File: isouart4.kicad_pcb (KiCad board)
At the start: 2 copper layers, 89 x 99 mm, 86 parts, among them J1 USB_B, J2 Conn_01x04, J3 Conn_01x04, J4 Conn_01x04, J5 Conn_01x04, U1 AMS1117-3.3, U10 74HC123, U11 74HC123, U2 π122U31, U3 π122U31, U4 π122U31, U5 π122U31, U7 CH344Q, U8 74HC123, U9 74HC123, Y1 8MHz

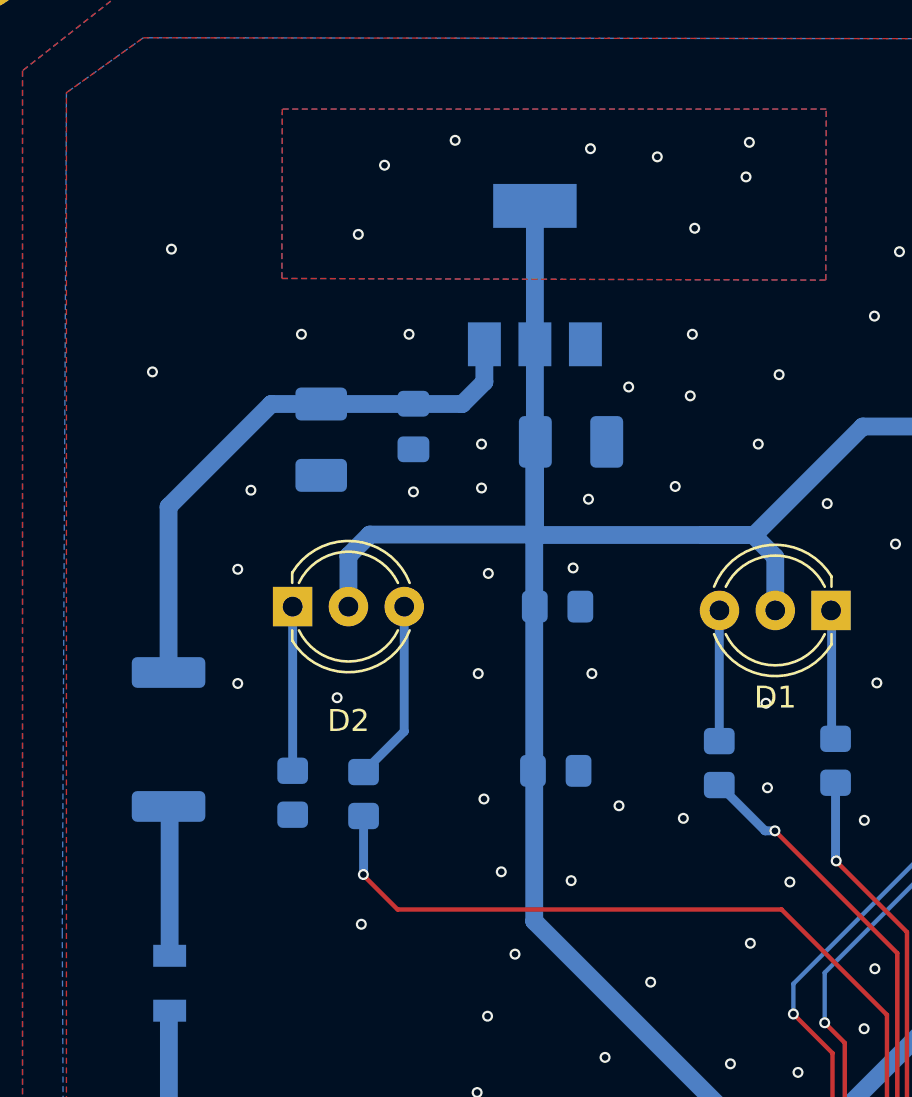
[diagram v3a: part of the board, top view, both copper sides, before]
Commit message: AMS1117-3.3 -> LP2950CDT-3.3 (reduce usb downstream capacitance)
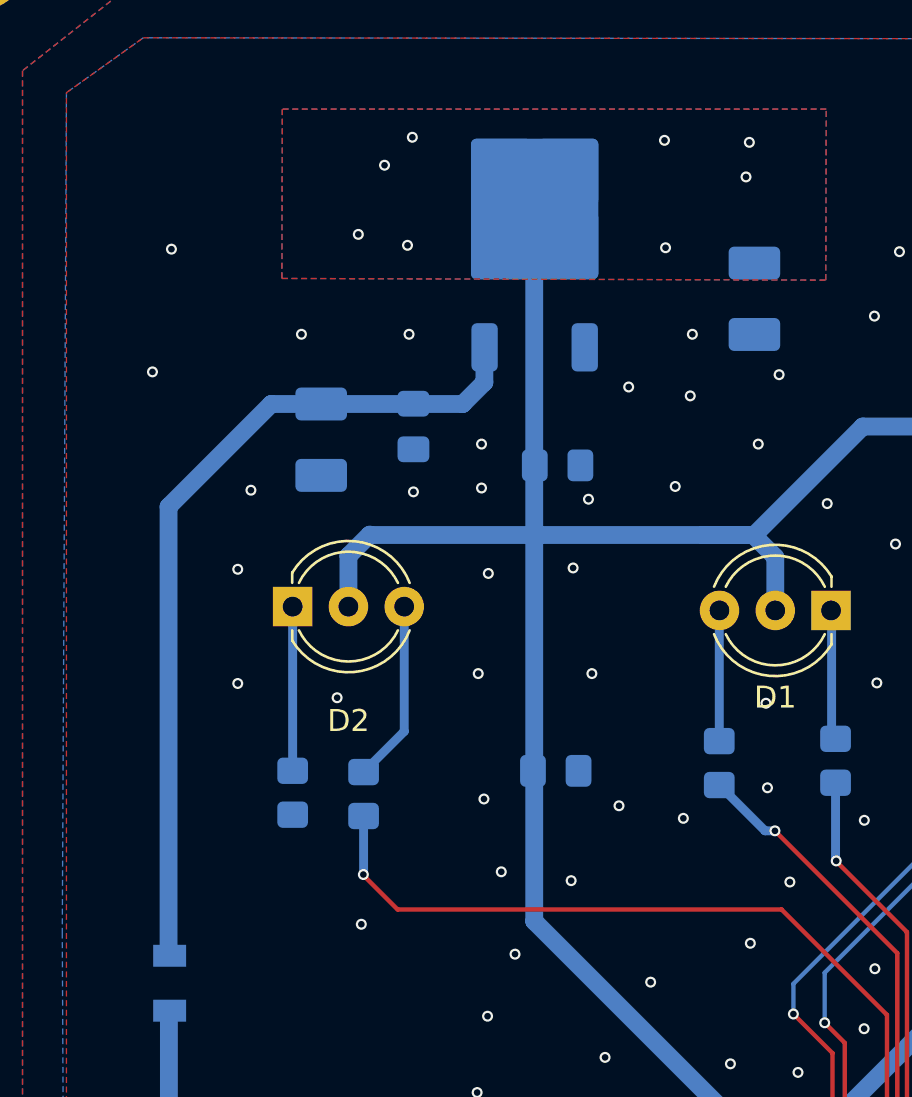
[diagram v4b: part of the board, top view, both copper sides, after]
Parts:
- removed R26: 4R3, Resistor_SMD:R_2512_6332Metric_Pad1.40x3.35mm_HandSolder
- C1: value 10uF -> 1uF
- C2: value 22uF -> 3.3uF
- F1: value 500mA -> 100mA
- U1: value AMS1117-3.3 -> LP2950CDT-3.3; footprint Package_TO_SOT_SMD:SOT-223-3_TabPin2 -> Package_TO_SOT_SMD:TO-252-2
- moved C2 10.6 mm to (179.3, 59.4), turned to -90 degrees
- moved C31 6.43 mm to (170.4, 67.0)
- moved U1 1.75 mm to (169.3, 56.6)
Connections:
- FB1 pad 1: Net-(FB1-Pad1) -> Net-(U1-VI)
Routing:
- net Net-(U1-VI): track 26.0 -> 39.0 mm
- net Net-(FB1-Pad1): track 6.82 -> 0.00 mm
- net /USB-UART4-CH344Q/VIN 3.3V: track 175.4 -> 171.5 mm

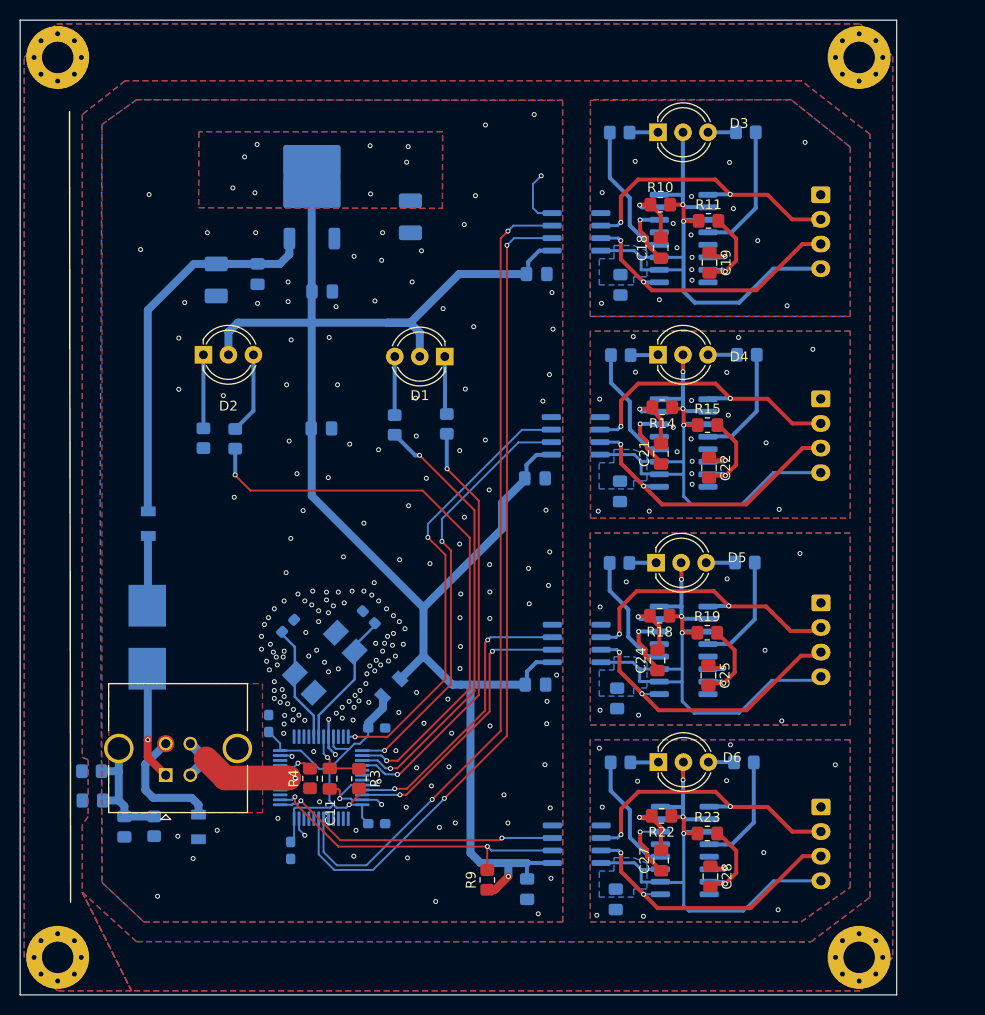
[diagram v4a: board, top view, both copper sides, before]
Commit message: adjust silkscreen and led positions; reannotate
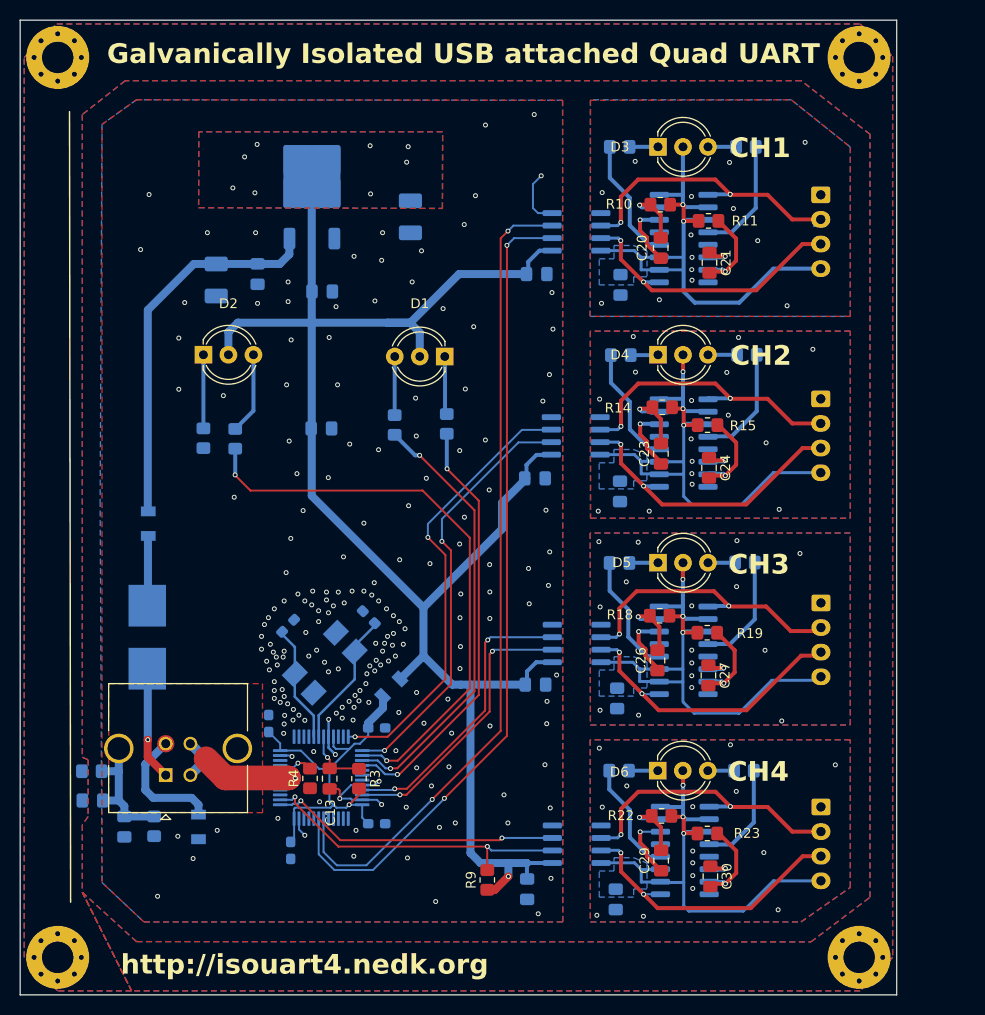
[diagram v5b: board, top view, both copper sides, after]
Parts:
- moved D3 1.48 mm to (204.5, 52.3)
- moved R12 1.48 mm to (213.4, 52.3)
- moved R13 1.46 mm to (200.6, 52.3)
- moved D6 0.87 mm to (204.4, 115.6)
- moved R25 0.85 mm to (200.5, 115.6)
- moved R24 0.84 mm to (213.2, 115.6)
- moved D5 0.19 mm to (204.5, 94.5)
- renumbered C8 to C10, C10 to C12, C11 to C13, C12 to C14, C13 to C15, C14 to C16, C15 to C17, C17 to C18, C16 to C19, C30 to C2, C18 to C20, C19 to C21, C20 to C22, C21 to C23, C22 to C24, C23 to C25, C24 to C26, C25 to C27, C26 to C28, C27 to C29, C31 to C3, C28 to C30, C29 to C31, C2 to C4, C3 to C5, C4 to C6, C5 to C7, C6 to C8, C7 to C9
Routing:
- net /indicators-ch1/V+MON: track 56.7 -> 55.2 mm
- net Net-(U8A-~{Q}): track 13.6 -> 12.1 mm
- net Net-(U8B-~{Q}): track 14.1 -> 12.6 mm
- net Net-(U11A-~{Q}): track 11.7 -> 10.8 mm
- net /indicators-ch4/V+MON: track 52.3 -> 51.5 mm
- net Net-(U11B-~{Q}): track 12.3 -> 11.5 mm
- net /indicators-ch4/GNDMON: vias 10 -> 15
- net /indicators-ch3/GNDMON: vias 8 -> 16
- net /indicators-ch2/GNDMON: vias 18 -> 16
- net /indicators-ch1/GNDMON: vias 16 -> 14
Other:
- board text added: "CH1"
- board text added: "CH2"
- board text added: "CH3"
- board text added: "CH4"
- board text added: "Galvanically Isolated USB attached Quad UART"
- board text added: "http://isouart4.nedk.org"

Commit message: Add OSHW logo
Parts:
- added REF1: OSHW, isouart4:OSHW, F.Cu at (149.9, 100.1)

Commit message: Adjust OSHW logo to have footprint and use it
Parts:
- removed REF1: OSHW, isouart4:OSHW
- added LOGO1: OSHW, isouart4:OSHW, F.Cu at (150.3, 99.9)

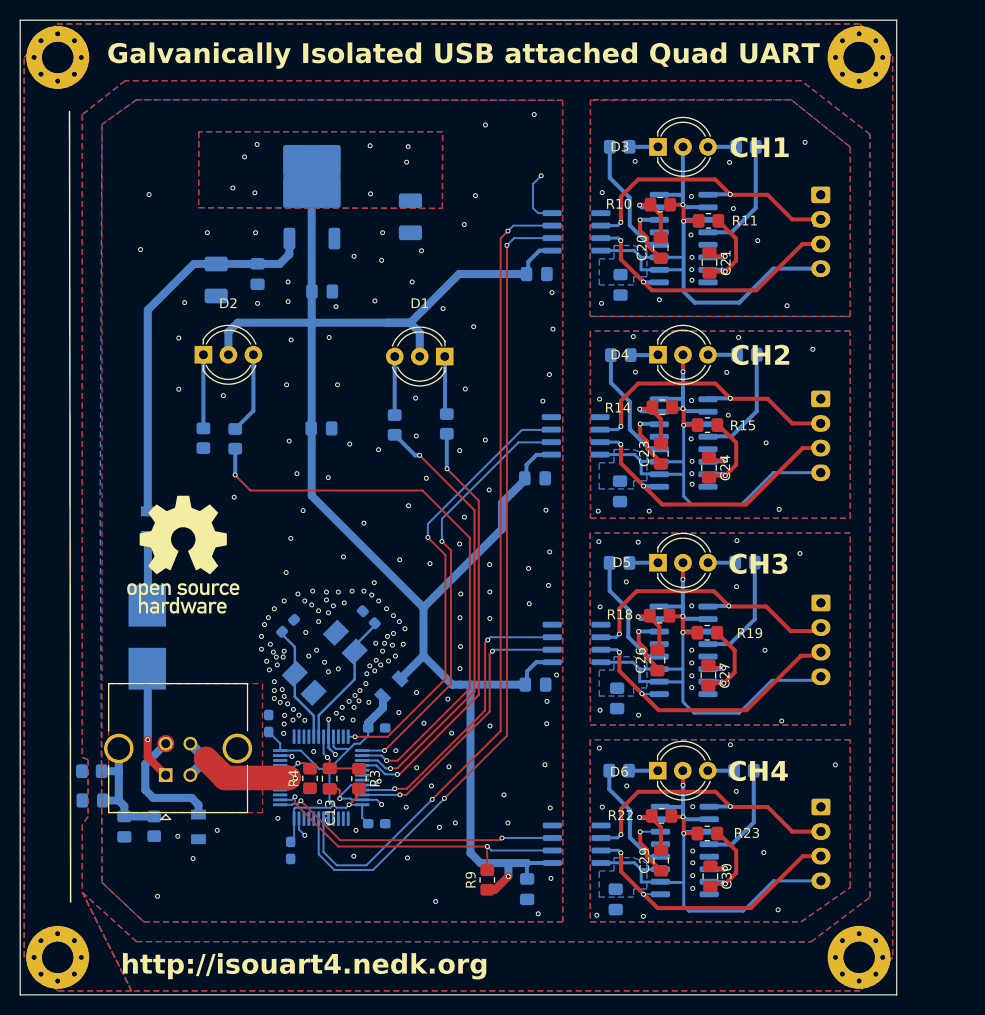
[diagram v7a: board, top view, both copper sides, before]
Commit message: increase via size to 0.6mm and via annular width to 0.13mm
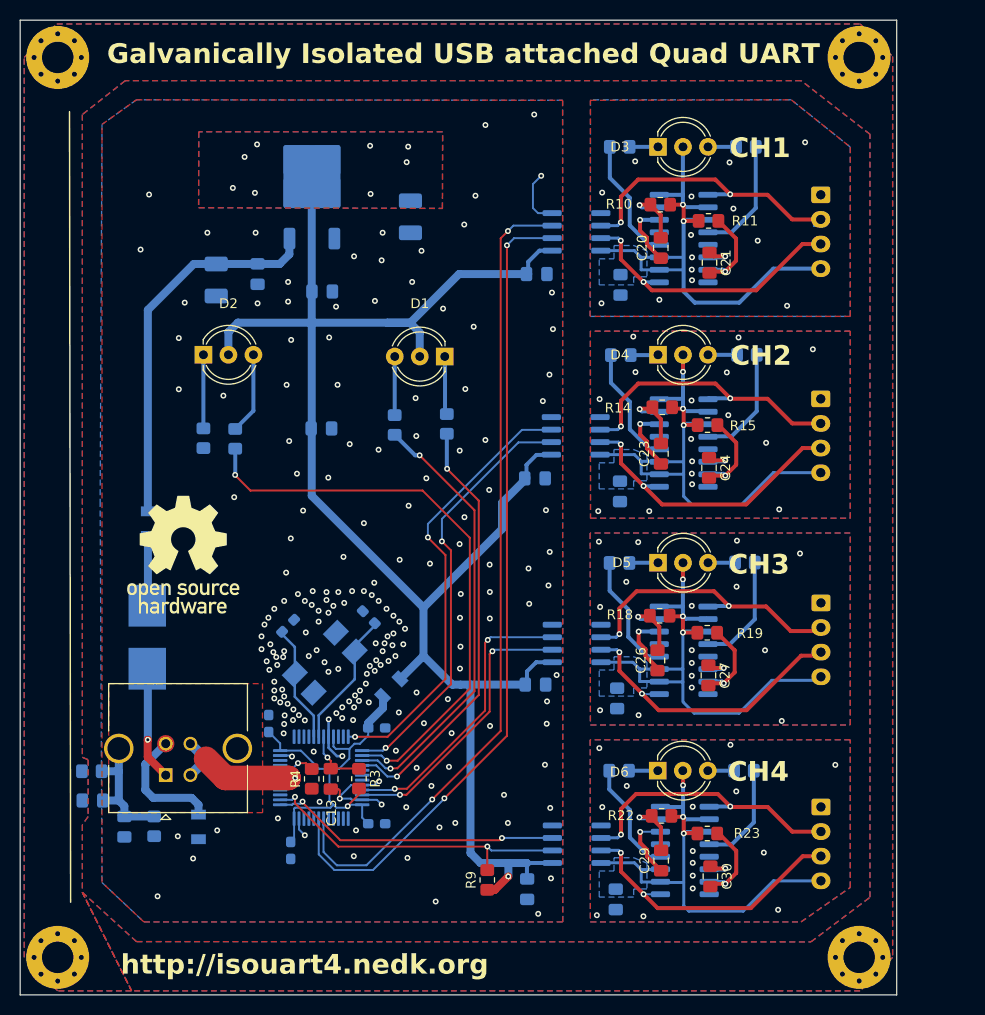
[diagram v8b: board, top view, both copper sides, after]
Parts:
- moved R4 0.18 mm to (169.3, 116.5)
- moved C13 0.11 mm to (171.2, 116.5)
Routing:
- net Net-(C14-Pad2): track 40.0 -> 40.7 mm
- net GND: track 35.1 -> 35.8 mm
